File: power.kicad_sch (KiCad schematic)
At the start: 6 parts, among them IC2 BQ21080YBGR, U2 TPS631000DRLR, U3 TPS62840DLCR

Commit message: Update
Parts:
- removed IC1: ~, footprints:SON40P150X150X50-9N, symbol XC6193:XC6193A103ER-G
- removed IC2: BQ21080YBGR, footprints:BGA8C40P2X4_100X155X50, symbol BQ21080YBGR:BQ21080YBGR
- removed U2: TPS631000DRLR, footprints:SOT50P160X60-8N, symbol TPS631000DRLR:TPS631000DRLR
- removed U3: TPS62840DLCR, footprints:SON50P200X150X100-8N, symbol TPS62840DLCR:TPS62840DLCR
- added U2: XC6193A103ER-G, footprints:SON40P150X150X50-9N, symbol XC6193:XC6193A103ER-G
- added U3: TPS631000DRLR, footprints:SOT50P160X60-8N, symbol TPS631000DRLR:TPS631000DRLR
- added U4: TPS62840DLCR, footprints:SON50P200X150X100-8N, symbol TPS62840DLCR:TPS62840DLCR
- added U5: BQ25185DLHR, footprints:SON40P220X200X80-11N, symbol BQ25185DLHR:BQ25185DLHR
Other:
- moved on the sheet: C1

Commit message: Update
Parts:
- removed C1: C, Capacitor_SMD:C_0402_1005Metric, symbol Device:C
- removed R1: 100K, Resistor_SMD:R_0402_1005Metric, symbol Device:R_US
- added C21, C22: 0.1uF, Capacitor_SMD:C_0402_1005Metric, symbol Device:C_US
- added C31, C32, C33: 22uF, Capacitor_SMD:C_0402_1005Metric, symbol Device:C_US
- added C41: 4.7uF, Capacitor_SMD:C_0402_1005Metric, symbol Device:C_US
- added C42, C51: 10uF, Capacitor_SMD:C_0402_1005Metric, symbol Device:C_US
- added C52, C53: 1uF, Capacitor_SMD:C_0402_1005Metric, symbol Device:C_US
- added L31: 1uH, Inductor_SMD:L_0402_1005Metric, symbol Device:L
- added L41: 2.2uH, Inductor_SMD:L_0402_1005Metric, symbol Device:L
- added R31, R32, R33, R41, R42: 100K, Resistor_SMD:R_0402_1005Metric, symbol Device:R_US
- added R34: 806K, Resistor_SMD:R_0402_1005Metric, symbol Device:R_US
- added R35: 91K, Resistor_SMD:R_0402_1005Metric, symbol Device:R_US
- added R43: 27K, Resistor_SMD:R_0402_1005Metric, symbol Device:R_US
- added R44: 240K, Resistor_SMD:R_0402_1005Metric, symbol Device:R_US
- added R51: 1K, Resistor_SMD:R_0402_1005Metric, symbol Device:R_US
- added R52: 5K, Resistor_SMD:R_0402_1005Metric, symbol Device:R_US
- added R53: 10K, Resistor_SMD:R_0402_1005Metric, symbol Device:R_US
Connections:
- net GND: now reaches U4.1 (GND)
- net GND: now also U2.2 (NC), U2.5 (VSS), U2.6 (TEST), U2.9 (EP), U3.7 (GND), U4.6 (STOP), U5.11 (EP), U5.4 (~{CE}), U5.5 (GND), C21.2, C22.2, C31.2, C32.2, C33.2, C41.2, C42.2, C51.2, C52.2, C53.2, R32.2, R35.2, R42.2, R43.2, R51.2, R52.2, R53.2
- net +5V_SYS: now reaches U4.2 (VIN)
- net +5V_SYS: now also U3.1 (VOUT), U4.4 (EN), C33.1, C41.1, R34.2, R41.2
- net at U4.3 (MODE): now also R41.1, R42.1
- net at U4.5 (VSET): now also R44.1
- net at U4.7 (SW): now also L41.2
- net +3.3V_SYS: now reaches U4.8 (VOS)
- net +3.3V_SYS: now also C42.1, L41.1
- net VCC_PRESYS: now reaches U5.1 (SYS)
- net VCC_PRESYS: now also U2.1 (VIN), C21.1, C51.1
- net +5V_USB: now reaches U5.10 (IN)
- net +5V_USB: now also C53.1
- net +BATT: now reaches U5.2 (BAT)
- net +BATT: now also C52.1
- net BAT_STAT_2: now reaches U5.3 (STAT2)
- net at U5.6 (TS/MR): now also R53.1
- net at U5.7 (ILIM/VSET): now also R52.1
- net at U5.8 (ISET): now also R51.1
- net BAT_STAT_1: now reaches U5.9 (STAT1)
- net SHDN: now reaches U2.7 (SHDN)
- net VCC_SYS: now reaches U2.8 (VOUT)
- net VCC_SYS: now also U3.4 (VIN), C22.1, C31.1, C32.1, R31.2, R33.2
- net at U3.2 (LX2): now also L31.2
- net at U3.3 (LX1): now also L31.1
- net at U3.5 (EN): now also R33.1
- net at U3.6 (MODE): now also R31.1, R32.1
- net at U3.8 (FB): now also R34.1, R35.1
- new net: R43.1, R44.2
- no-connect marks 0 -> 2
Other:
- moved on the sheet: U2, U3, U4, U5

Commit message: Update
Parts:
- added C23: 0.1uF, Capacitor_SMD:C_0402_1005Metric, symbol Device:C_US
- added R21: 5K, Resistor_SMD:R_0402_1005Metric, symbol Device:R_US
- added R22: 200K, Resistor_SMD:R_0402_1005Metric, symbol Device:R_US
- added S5: SKRTLAE010, footprints:SKRTLAE010, symbol SKRTLAE010:SKRTLAE010
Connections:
- net GND: now also C23.2, R21.2, S5.1, S5.3, S5.MP1, S5.MP2
- net SHDN: now also C23.1, R21.1
- net VCC_PRESYS: now also R22.2
- net SW: now reaches U2.3 (SW)
- net SW: now also R22.1, S5.2
- no-connect marks 2 -> 1
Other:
- moved on the sheet: C21, C22

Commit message: Update
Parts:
- added S6: SKRTLAE010, footprints:SKRTLAE010, symbol SKRTLAE010:SKRTLAE010
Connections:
- net GND: now also S6.1, S6.3, S6.MP1, S6.MP2
- net SW: now also S6.2
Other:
- moved on the sheet: C51, C52, C53, R22, R51, R52, R53, S5, U5

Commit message: Update
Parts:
- added D3: RB751S40,115, footprints:RB751S40115, symbol RB751S40_115:RB751S40,115
- added R23: 47K, Resistor_SMD:R_0402_1005Metric, symbol Device:R_US
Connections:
- net +3.3V_SYS: now also R23.2
- net SW: now also D3.2 (A)
- new net SW_P: D3.1 (K), R23.1
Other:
- moved on the sheet: C21, C22, C23, R21, R22, U2

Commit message: Fix global nets
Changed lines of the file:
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@@
-	(wire
-		(pts
-			(xy 34.29 53.34) (xy 49.53 53.34)
-		)
-		(stroke
-			(width 0)
-			(type default)
-		)
-	)
 	(wire
 		(pts
@@
 	(wire
 		(pts
-			(xy 226.06 116.84) (xy 238.76 116.84)
-		)
-		(stroke
-			(width 0)
-			(type default)
-		)
-	)
-	(wire
-		(pts
 			(xy 92.71 26.67) (xy 92.71 39.37)
 		)
@@
 	(wire
 		(pts
+			(xy 90.17 44.45) (xy 102.87 44.45)
+		)
+		(stroke
+			(width 0)
+			(type default)
+		)
+	)
+	(wire
+		(pts
 			(xy 81.28 124.46) (xy 81.28 137.16)
 		)
@@
 	(wire
 		(pts
-			(xy 226.06 119.38) (xy 238.76 119.38)
-		)
-		(stroke
-			(width 0)
-			(type default)
-		)
-	)
-	(wire
-		(pts
 			(xy 219.71 129.54) (xy 229.87 129.54)
 		)
@@
 	(wire
 		(pts
+			(xy 33.02 53.34) (xy 49.53 53.34)
+		)
+		(stroke
+			(width 0)
+			(type default)
+		)
+	)
+	(wire
+		(pts
 			(xy 208.28 64.77) (xy 210.82 64.77)
 		)
@@
 	(wire
 		(pts
-			(xy 91.44 44.45) (xy 102.87 44.45)
-		)
-		(stroke
-			(width 0)
-			(type default)
-		)
-	)
-	(wire
-		(pts
 			(xy 77.47 85.09) (xy 77.47 82.55)
 		)
@@
 			(width 0)
 			(type default)
-		)
-	)
-	(label "SHDN"
-		(at 91.44 44.45 0)
-		(effects
-			(font
-				(size 1.27 1.27)
-			)
-			(justify left bottom)
-		)
-	)
-	(label "BAT_STAT_1"
-		(at 226.06 116.84 0)
-		(effects
-			(font
-				(size 1.27 1.27)
-			)
-			(justify left bottom)
-		)
-	)
-	(label "BAT_STAT_2"
-		(at 226.06 119.38 0)
-		(effects
-			(font
-				(size 1.27 1.27)
-			)
-			(justify left bottom)
 		)
 	)
@@
 		)
 	)
-	(label "SW_P"
-		(at 34.29 53.34 0)
-		(effects
-			(font
-				(size 1.27 1.27)
-			)
-			(justify left bottom)
-		)
-	)
 	(label "SW"
 		(at 74.93 74.93 0)
@@
 		)
 	)
+	(global_label "SW_P"
+		(shape input)
+		(at 33.02 53.34 180)
+		(fields_autoplaced yes)
+		(effects
+			(font
+				(size 1.27 1.27)
+			)
+			(justify right)
+		)
+		(property "Intersheetrefs" "${INTERSHEET_REFS}"
+			(at 25.1363 53.34 0)
+			(effects
+				(font
+					(size 1.27 1.27)
+				)
+				(justify right)
+				(hide yes)
+			)
+		)
+	)
+	(global_label "SHDN"
+		(shape input)
+		(at 90.17 44.45 180)
+		(fields_autoplaced yes)
+		(effects
+			(font
+				(size 1.27 1.27)
+			)
+			(justify right)
+		)
+		(property "Intersheetrefs" "${INTERSHEET_REFS}"
+			(at 82.0443 44.45 0)
+			(effects
+				(font
+					(size 1.27 1.27)
+				)
+				(justify right)
+				(hide yes)
+			)
+		)
+	)
+	(global_label "BAT_STAT_1"
+		(shape input)
+		(at 238.76 116.84 180)
+		(fields_autoplaced yes)
+		(effects
+			(font
+				(size 1.27 1.27)
+			)
+			(justify right)
+		)
+		(property "Intersheetrefs" "${INTERSHEET_REFS}"
+			(at 225.0706 116.84 0)
+			(effects
+				(font
+					(size 1.27 1.27)
+				)
+				(justify right)
+				(hide yes)
+			)
+		)
+	)
+	(global_label "BAT_STAT_2"
+		(shape input)
+		(at 238.76 119.38 180)
+		(fields_autoplaced yes)
+		(effects
+			(font
+				(size 1.27 1.27)
+			)
+			(justify right)
+		)
+		(property "Intersheetrefs" "${INTERSHEET_REFS}"
+			(at 225.0706 119.38 0)
+			(effects
+				(font
+					(size 1.27 1.27)
+				)
+				(justify right)
+				(hide yes)
+			)
+		)
+	)

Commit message: Place components
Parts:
- added J11: Conn_01x02_MountingPin, Connector_JST:JST_SH_BM02B-SRSS-TB_1x02-1MP_P1.00mm_Vertical, symbol Connector_Generic_MountingPin:Conn_01x02_MountingPin
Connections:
- net +BATT: now also J11.1 (Pin_1)
- net GND: now also J11.2 (Pin_2), J11.MP (MountPin)
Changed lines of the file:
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@@
 	)
 	(junction
+		(at 157.48 154.94)
+		(diameter 0)
+		(color 0 0 0 0)
+	)
+	(junction
 		(at 81.28 137.16)
 		(diameter 0)
@@
 	(wire
 		(pts
+			(xy 157.48 154.94) (xy 162.56 154.94)
+		)
+		(stroke
+			(width 0)
+			(type default)
+		)
+	)
+	(wire
+		(pts
 			(xy 78.74 148.59) (xy 81.28 148.59)
 		)
@@
 	(wire
 		(pts
+			(xy 157.48 154.94) (xy 157.48 156.21)
+		)
+		(stroke
+			(width 0)
+			(type default)
+		)
+	)
+	(wire
+		(pts
 			(xy 220.98 91.44) (xy 226.06 91.44)
 		)
@@
 	(wire
 		(pts
+			(xy 157.48 149.86) (xy 157.48 154.94)
+		)
+		(stroke
+			(width 0)
+			(type default)
+		)
+	)
+	(wire
+		(pts
 			(xy 73.66 53.34) (xy 73.66 41.91)
 		)
@@
 	)
 	(symbol
+		(lib_id "power:+BATT")
+		(at 157.48 147.32 90)
+		(unit 1)
+		(exclude_from_sim no)
+		(in_bom yes)
+		(on_board yes)
+		(dnp no)
+		(fields_autoplaced yes)
+		(property "Reference" "#PWR097"
+			(at 161.29 147.32 0)
+			(effects
+				(font
+					(size 1.27 1.27)
+				)
+				(hide yes)
+			)
+		)
+		(property "Value" "+BATT"
+			(at 153.67 147.3199 90)
+			(effects
+				(font
+					(size 1.27 1.27)
+				)
+				(justify left)
+			)
+		)
+		(property "Footprint" ""
+			(at 157.48 147.32 0)
+			(effects
+				(font
+					(size 1.27 1.27)
+				)
+				(hide yes)
+			)
+		)
+		(property "Datasheet" ""
+			(at 157.48 147.32 0)
+			(effects
+				(font
+					(size 1.27 1.27)
+				)
+				(hide yes)
+			)
+		)
+		(property "Description" "Power symbol creates a global label with name \"+BATT\""
+			(at 157.48 147.32 0)
+			(effects
+				(font
+					(size 1.27 1.27)
+				)
+				(hide yes)
+			)
+		)
+		(pin "1"
+		)
+		(instances
+			(project "ykb-dactyl-v1"
+				(path "/e14fa40b-de41-4d68-adfe-82a50bad5819/3a08b8c2-5472-461f-8ded-0be9796eaa52"
+					(reference "#PWR097")
+					(unit 1)
+				)
+			)
+		)
+	)
+	(symbol
 		(lib_id "TPS631000DRLR:TPS631000DRLR")
 		(at 241.3 77.47 0)
@@
 					(unit 1)
 				)
+			)
+		)
+	)
+	(symbol
+		(lib_id "Connector_Generic_MountingPin:Conn_01x02_MountingPin")
+		(at 162.56 147.32 0)
+		(unit 1)
+		(exclude_from_sim no)
+		(in_bom yes)
+		(on_board yes)
+		(dnp no)
+		(fields_autoplaced yes)
+		(property "Reference" "J11"
+			(at 165.1 147.6755 0)
+			(effects
+				(font
+					(size 1.27 1.27)
+				)
+				(justify left)
+			)
+		)
+		(property "Value" "Conn_01x02_MountingPin"
+			(at 165.1 150.2155 0)
+			(effects
+				(font
+					(size 1.27 1.27)
+				)
+				(justify left)
+			)
+		)
+		(property "Footprint" "Connector_JST:JST_SH_BM02B-SRSS-TB_1x02-1MP_P1.00mm_Vertical"
+			(at 162.56 147.32 0)
+			(effects
+				(font
+					(size 1.27 1.27)
+				)
+				(hide yes)
+			)
+		)
+		(property "Datasheet" "~"
+			(at 162.56 147.32 0)
+			(effects
+				(font
+					(size 1.27 1.27)
+				)
+				(hide yes)
+			)
+		)
+		(property "Description" "Generic connectable mounting pin connector, single row, 01x02, script generated (kicad-library-utils/schlib/autogen/connector/)"
+			(at 162.56 147.32 0)
+			(effects
+				(font
+					(size 1.27 1.27)
+				)
+				(hide yes)
+			)
+		)
+		(pin "1"
+		)
+		(pin "MP"
+		)
+		(pin "2"
+		)
+		(instances
+			(project ""
+				(path "/e14fa40b-de41-4d68-adfe-82a50bad5819/3a08b8c2-5472-461f-8ded-0be9796eaa52"
+					(reference "J11")
+					(unit 1)
+				)
+			)
+		)
+	)
+	(symbol
+		(lib_id "power:GND")
+		(at 157.48 156.21 0)
+		(unit 1)
+		(exclude_from_sim no)
+		(in_bom yes)
+		(on_board yes)
+		(dnp no)
+		(fields_autoplaced yes)
+		(property "Reference" "#PWR098"
+			(at 157.48 162.56 0)
+			(effects
+				(font
+					(size 1.27 1.27)
+				)
+				(hide yes)
+			)
+		)
+		(property "Value" "GND"
+			(at 157.48 161.29 0)
+			(effects
+				(font
+					(size 1.27 1.27)
+				)
+			)
+		)
+		(property "Footprint" ""
+			(at 157.48 156.21 0)
+			(effects
+				(font
+					(size 1.27 1.27)
+				)
+				(hide yes)
+			)
+		)
+		(property "Datasheet" ""
+			(at 157.48 156.21 0)
+			(effects
+				(font
+					(size 1.27 1.27)
+				)
+				(hide yes)
+			)
+		)
+		(property "Description" "Power symbol creates a global label with name \"GND\" , ground"
+			(at 157.48 156.21 0)
+			(effects
+				(font
+					(size 1.27 1.27)
+				)
+				(hide yes)
+			)
+		)
+		(pin "1"
+		)
+		(instances
+			(project "ykb-dactyl-v1"
+				(path "/e14fa40b-de41-4d68-adfe-82a50bad5819/3a08b8c2-5472-461f-8ded-0be9796eaa52"
+					(reference "#PWR098")
+					(unit 1)
+				)

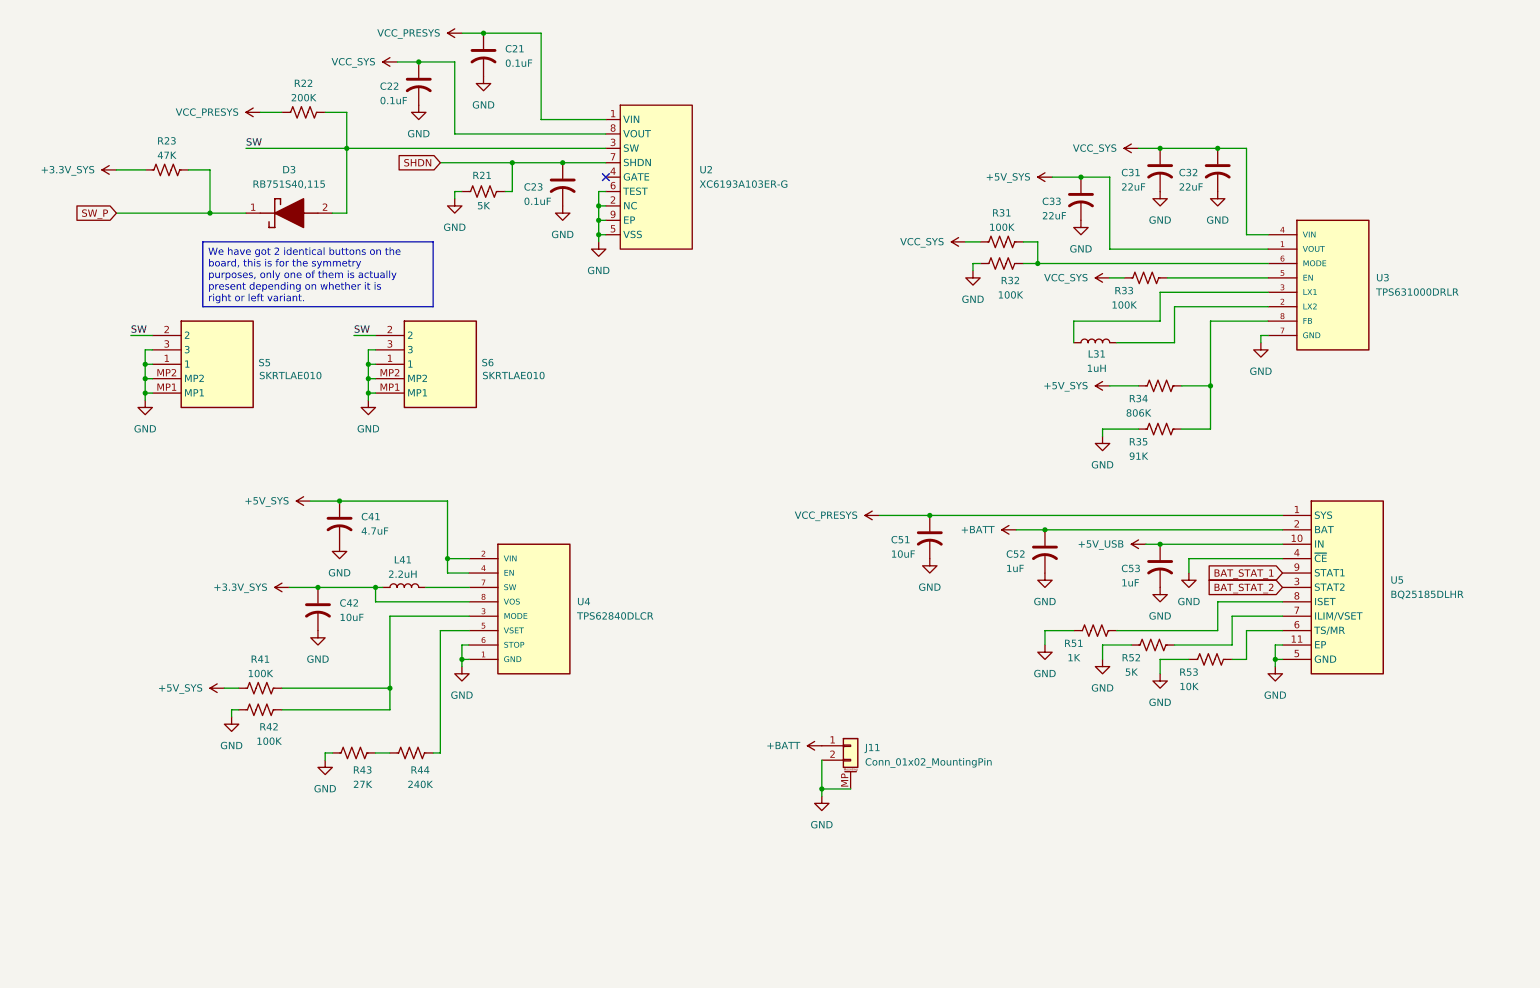
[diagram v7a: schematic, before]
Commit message: Trace the board
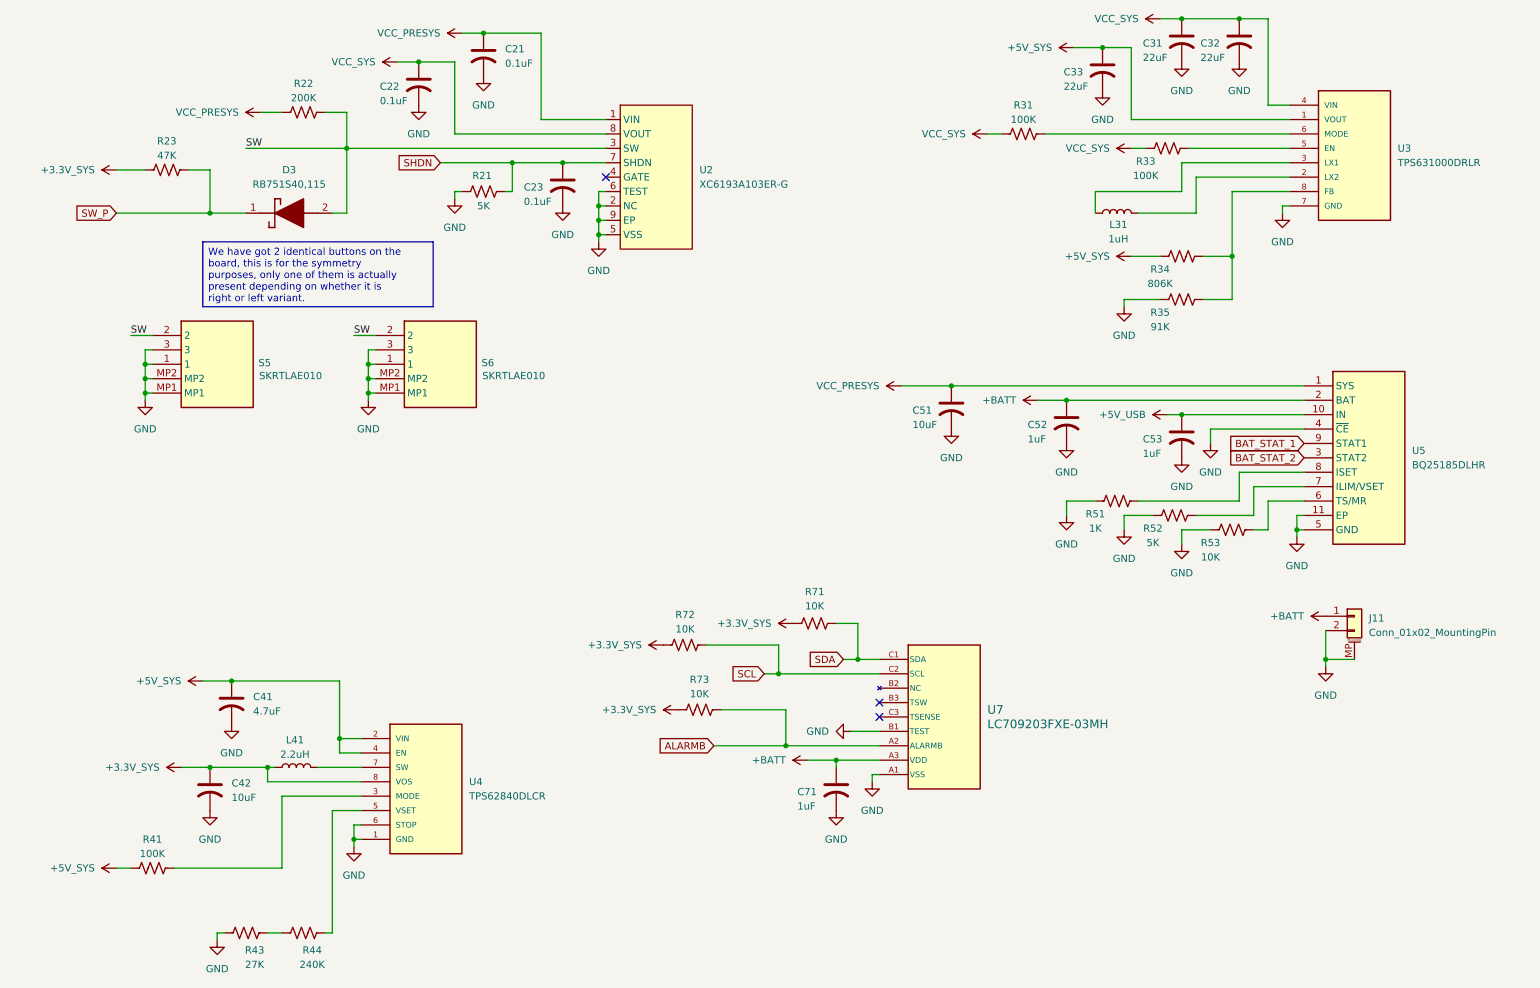
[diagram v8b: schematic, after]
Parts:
- removed R32, R42: 100K, Resistor_SMD:R_0402_1005Metric, symbol Device:R_US
- added C71: 1uF, Capacitor_SMD:C_0402_1005Metric, symbol Device:C_US
- added R71, R72, R73: 10K, Resistor_SMD:R_0402_1005Metric, symbol Device:R_US
- added U7: LC709203FXE-03MH, footprints:WLCSP9_1P60X1P76_ONS, symbol 2026-03-20_21-20-11:LC709203FXE-03MH
- J11: footprint Connector_JST:JST_SH_BM02B-SRSS-TB_1x02-1MP_P1.00mm_Vertical -> Connector_JST:JST_SHL_SM02B-SHLS-TF_1x02-1MP_P1.00mm_Horizontal
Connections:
- net +3.3V_SYS: now also R71.2, R72.2, R73.2
- net +BATT: now also C71.1, U7.A3 (VDD)
- net GND: now also C71.2, U7.A1 (VSS), U7.B1 (TEST)
- new net ALARMB: R73.1, U7.A2 (ALARMB)
- new net SCL: R72.1, U7.C2 (SCL)
- new net SDA: R71.1, U7.C1 (SDA)
- no-connect marks 1 -> 3
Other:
- moved on the sheet: C31, C32, C33, C41, C42, C51, C52, C53, J11, L31, L41, R31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
